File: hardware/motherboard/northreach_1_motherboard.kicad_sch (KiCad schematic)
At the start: 21 parts, among them J1 USB_C_Receptacle, J2 Conn_01x03_Pin, J3 Conn_01x20, J4 Conn_01x03_Pin, SW1 SW_Push, SW2 SW_Push, U1 TPS7A4701xRGW, U2 ESP32-S3-MINI-1U

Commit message: kicad: add LCSC parts
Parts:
- C1: LCSC (none) -> C28323
- C2, C5: LCSC (none) -> C15850
- C3, C4: LCSC (none) -> C28233
- J1: LCSC (none) -> C5119948
- J3: LCSC (none) -> C596730
- R1, R2: LCSC (none) -> C84375
- R3, R4: LCSC (none) -> C84376
- U1: LCSC (none) -> C90084
- U2: LCSC (none) -> C2980299
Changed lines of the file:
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@@
+			)
+		)
+		(property "LCSC" "C596730"
+			(at 121.92 114.3 0)
+			(effects
+				(font
+					(size 1.27 1.27)
+				)
+				(hide yes)
 			)
 		)
@@
 			)
 		)
+		(property "LCSC" "C2980299"
+			(at 232.41 113.03 0)
+			(effects
+				(font
+					(size 1.27 1.27)
+				)
+				(hide yes)
+			)
+		)
 		(pin "10"
 		)
@@
 		)
 		(property "Description" "Unpolarized capacitor"
+			(at 228.6 77.47 0)
+			(effects
+				(font
+					(size 1.27 1.27)
+				)
+				(hide yes)
+			)
+		)
+		(property "LCSC" "C28233"
 			(at 228.6 77.47 0)
 			(effects
@@
 			)
 		)
+		(property "LCSC" "C90084"
+			(at 62.23 160.02 0)
+			(effects
+				(font
+					(size 1.27 1.27)
+				)
+				(hide yes)
+			)
+		)
 		(pin "1"
 		)
@@
 			)
 		)
+		(property "LCSC" "C5119948"
+			(at 45.72 67.31 0)
+			(effects
+				(font
+					(size 1.27 1.27)
+				)
+				(hide yes)
+			)
+		)
 		(pin "A11"
 		)
@@
 			)
 		)
+		(property "LCSC" "C84375"
+			(at 73.66 45.72 90)
+			(effects
+				(font
+					(size 1.27 1.27)
+				)
+				(hide yes)
+			)
+		)
 		(pin "2"
 		)
@@
 		)
 		(property "Description" "Unpolarized capacitor"
+			(at 125.73 40.64 0)
+			(effects
+				(font
+					(size 1.27 1.27)
+				)
+				(hide yes)
+			)
+		)
+		(property "LCSC" "C28233"
 			(at 125.73 40.64 0)
 			(effects
@@
 			)
 		)
+		(property "LCSC" "C84376"
+			(at 118.11 35.56 90)
+			(effects
+				(font
+					(size 1.27 1.27)
+				)
+				(hide yes)
+			)
+		)
 		(pin "2"
 		)
@@
 			)
 		)
+		(property "LCSC" "C84376"
+			(at 123.19 58.42 90)
+			(effects
+				(font
+					(size 1.27 1.27)
+				)
+				(hide yes)
+			)
+		)
 		(pin "2"
 		)
@@
 			)
 		)
+		(property "LCSC" "C15850"
+			(at 228.6 66.04 0)
+			(effects
+				(font
+					(size 1.27 1.27)
+				)
+				(hide yes)
+			)
+		)
 		(pin "1"
 		)
@@
 			)
 		)
+		(property "LCSC" "C84375"
+			(at 73.66 50.8 90)
+			(effects
+				(font
+					(size 1.27 1.27)
+				)
+				(hide yes)
+			)
+		)
 		(pin "2"
 		)
@@
 			)
 		)
+		(property "LCSC" "C28323"
+			(at 77.47 173.99 0)
+			(effects
+				(font
+					(size 1.27 1.27)
+				)
+				(hide yes)
+			)
+		)
 		(pin "1"
 		)
@@
 			(at 38.1 153.67 0)
 			(effects
+				(font
+					(size 1.27 1.27)
+				)
+				(hide yes)
+			)
+		)
+		(property "LCSC" "C15850"
+			(at 38.1 153.67 0)
+			(effects

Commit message: schematic: motherboard: change switch footprint for EN and RESET
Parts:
- SW1, SW2: footprint Button_Switch_THT:SW_PUSH_6mm_H5mm -> Button_Switch_THT:SW_PUSH_6mm_H4.3mm
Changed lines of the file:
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@@
 			)
 		)
-		(property "Footprint" "Button_Switch_THT:SW_PUSH_6mm_H5mm"
+		(property "Footprint" "Button_Switch_THT:SW_PUSH_6mm_H4.3mm"
 			(at 137.16 40.64 0)
 			(effects
@@
 			)
 		)
-		(property "Footprint" "Button_Switch_THT:SW_PUSH_6mm_H5mm"
+		(property "Footprint" "Button_Switch_THT:SW_PUSH_6mm_H4.3mm"
 			(at 128.27 64.77 0)
 			(effects

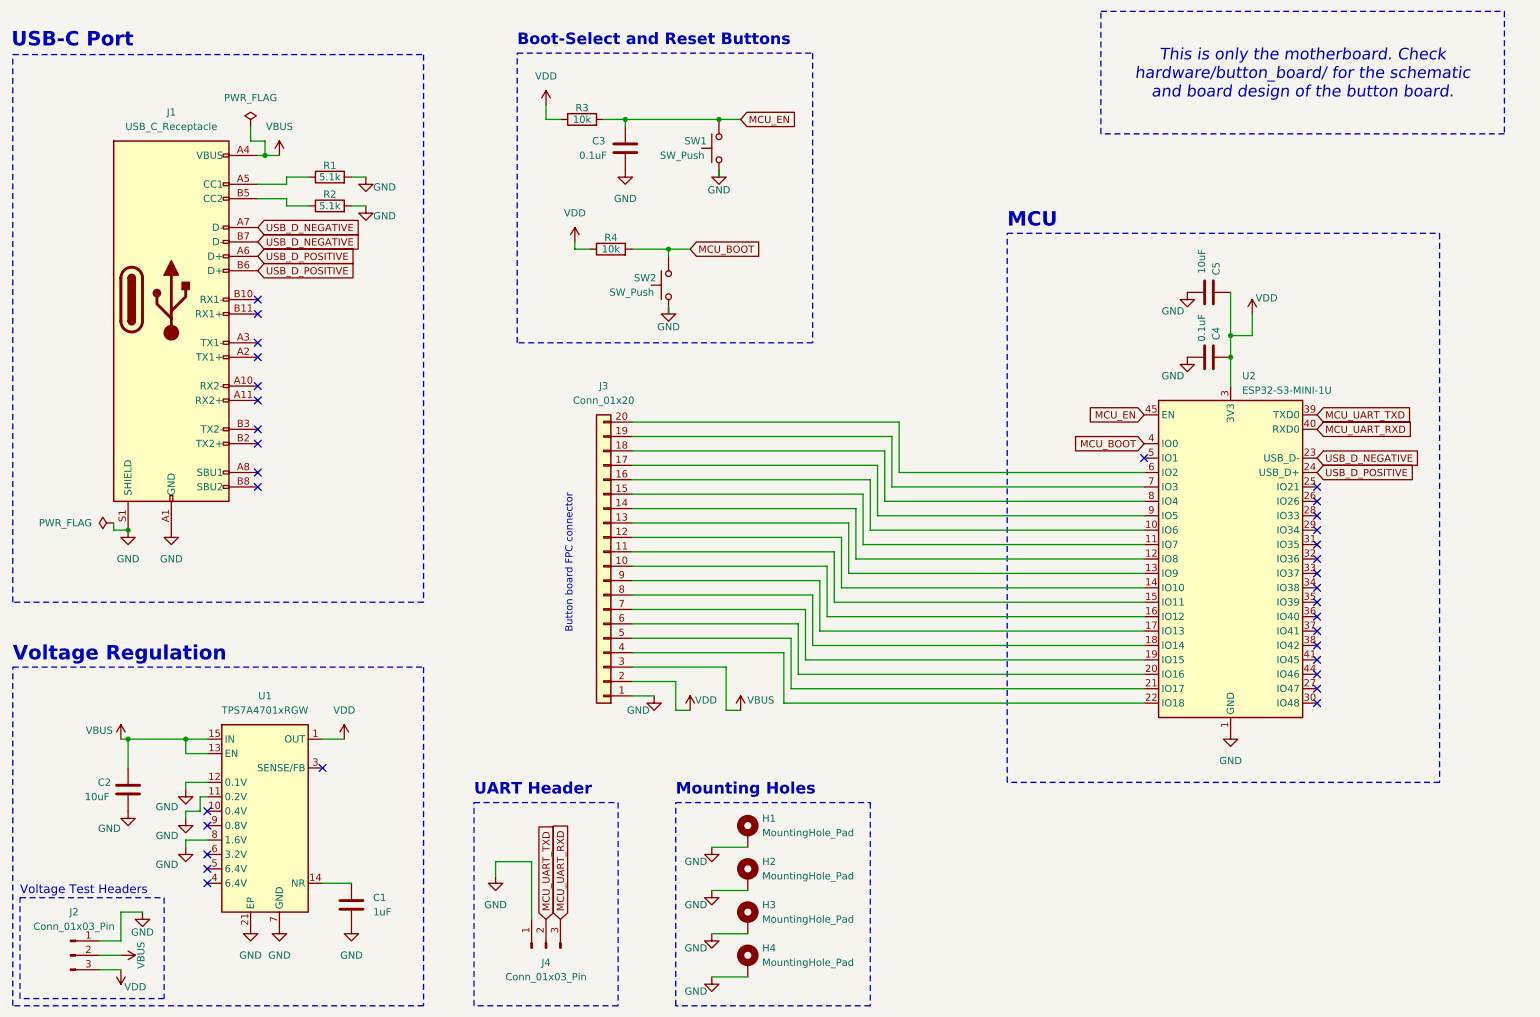
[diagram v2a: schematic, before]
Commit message: schematic: motherboard: add usb esd protection
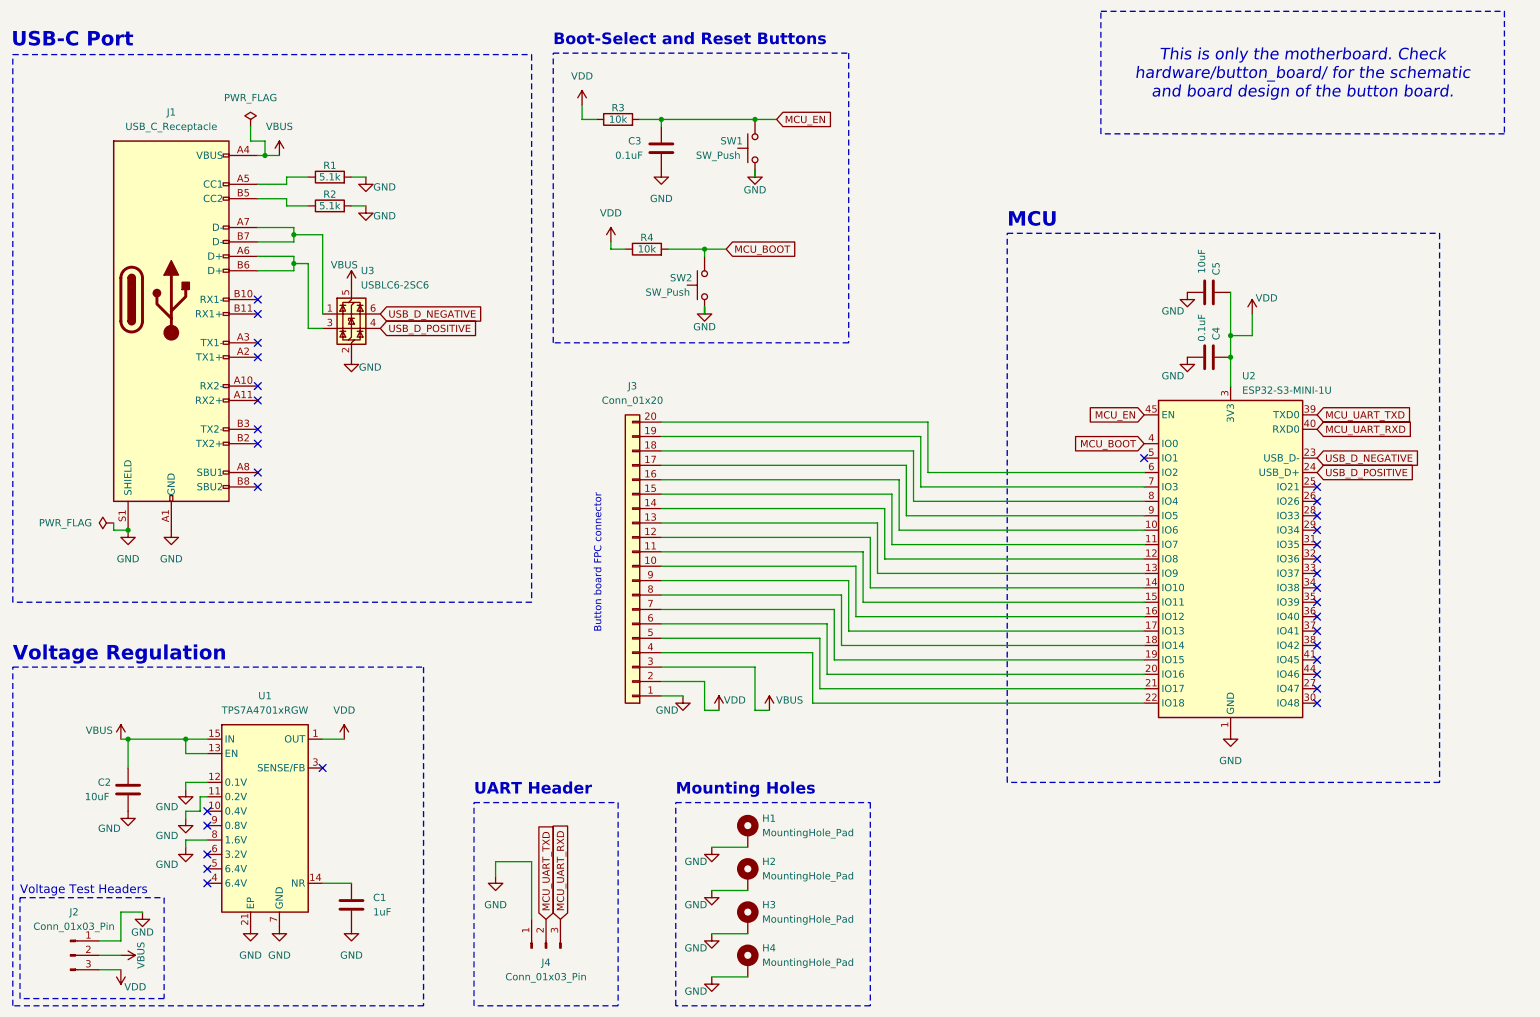
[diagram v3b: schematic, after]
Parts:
- added U3: USBLC6-2SC6, Package_TO_SOT_SMD:SOT-23-6, symbol Power_Protection:USBLC6-2SC6
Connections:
- net GND: now also U3.2 (GND)
- net USB_D_NEGATIVE: now also U3.6 (I/O1); no longer J1.A7 (D-), J1.B7 (D-)
- net USB_D_POSITIVE: now also U3.4 (I/O2); no longer J1.A6 (D+), J1.B6 (D+)
- net VBUS: now also U3.5 (VBUS)
- new net: J1.A6 (D+), J1.B6 (D+), U3.3 (I/O2)
- new net: J1.A7 (D-), J1.B7 (D-), U3.1 (I/O1)
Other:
- moved on the sheet: C3, J3, R3, R4, SW1, SW2

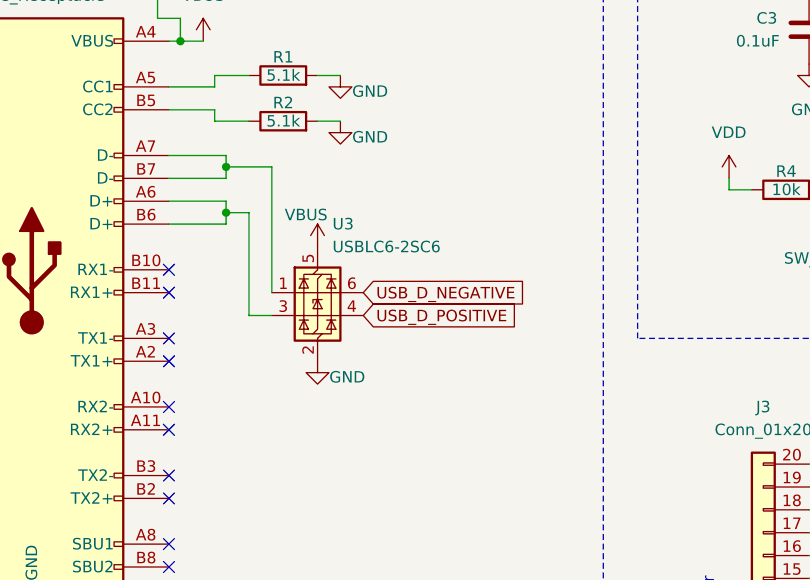
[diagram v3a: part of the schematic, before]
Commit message: schematic: motherboard: text, drawing sheet details
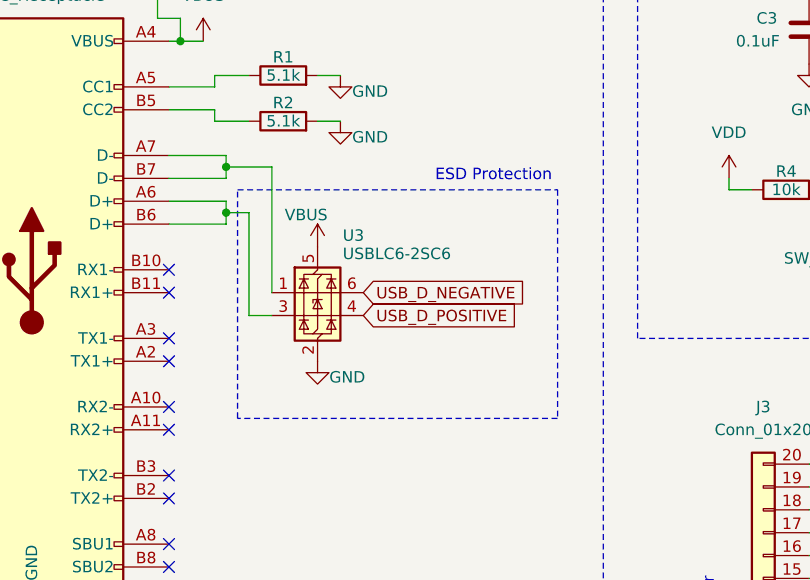
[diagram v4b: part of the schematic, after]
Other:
- note added: "ESD Protection"
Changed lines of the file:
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@@
 	(title_block
 		(title "NorthReach 1 - Motherboard")
-		(date "2026-01-08")
+		(date "2026-01-24")
 		(rev "v1.0")
 		(company "Stratos Thivaios")
@@
 	)
 	(rectangle
+		(start 68.58 58.42)
+		(end 104.14 83.82)
+		(stroke
+			(width 0)
+			(type dash_dot)
+			(color 0 1 255 1)
+		)
+		(fill
+			(type none)
+		)
+	)
+	(rectangle
 		(start 17.78 132.08)
 		(end 90.17 191.77)
@@
 		)
 	)
+	(text "ESD Protection"
+		(exclude_from_sim no)
+		(at 97.028 56.896 0)
+		(effects
+			(font
+				(size 1.27 1.27)
+			)
+		)
+	)
 	(text "USB-C Port"
 		(exclude_from_sim no)
@@
 		(on_board yes)
 		(dnp no)
-		(fields_autoplaced yes)
 		(property "Reference" "U3"
-			(at 79.1211 62.23 0)
+			(at 80.264 63.5 0)
 			(effects
 				(font
@@
 		)
 		(property "Value" "USBLC6-2SC6"
-			(at 79.1211 64.77 0)
+			(at 80.264 65.532 0)
 			(effects
 				(font

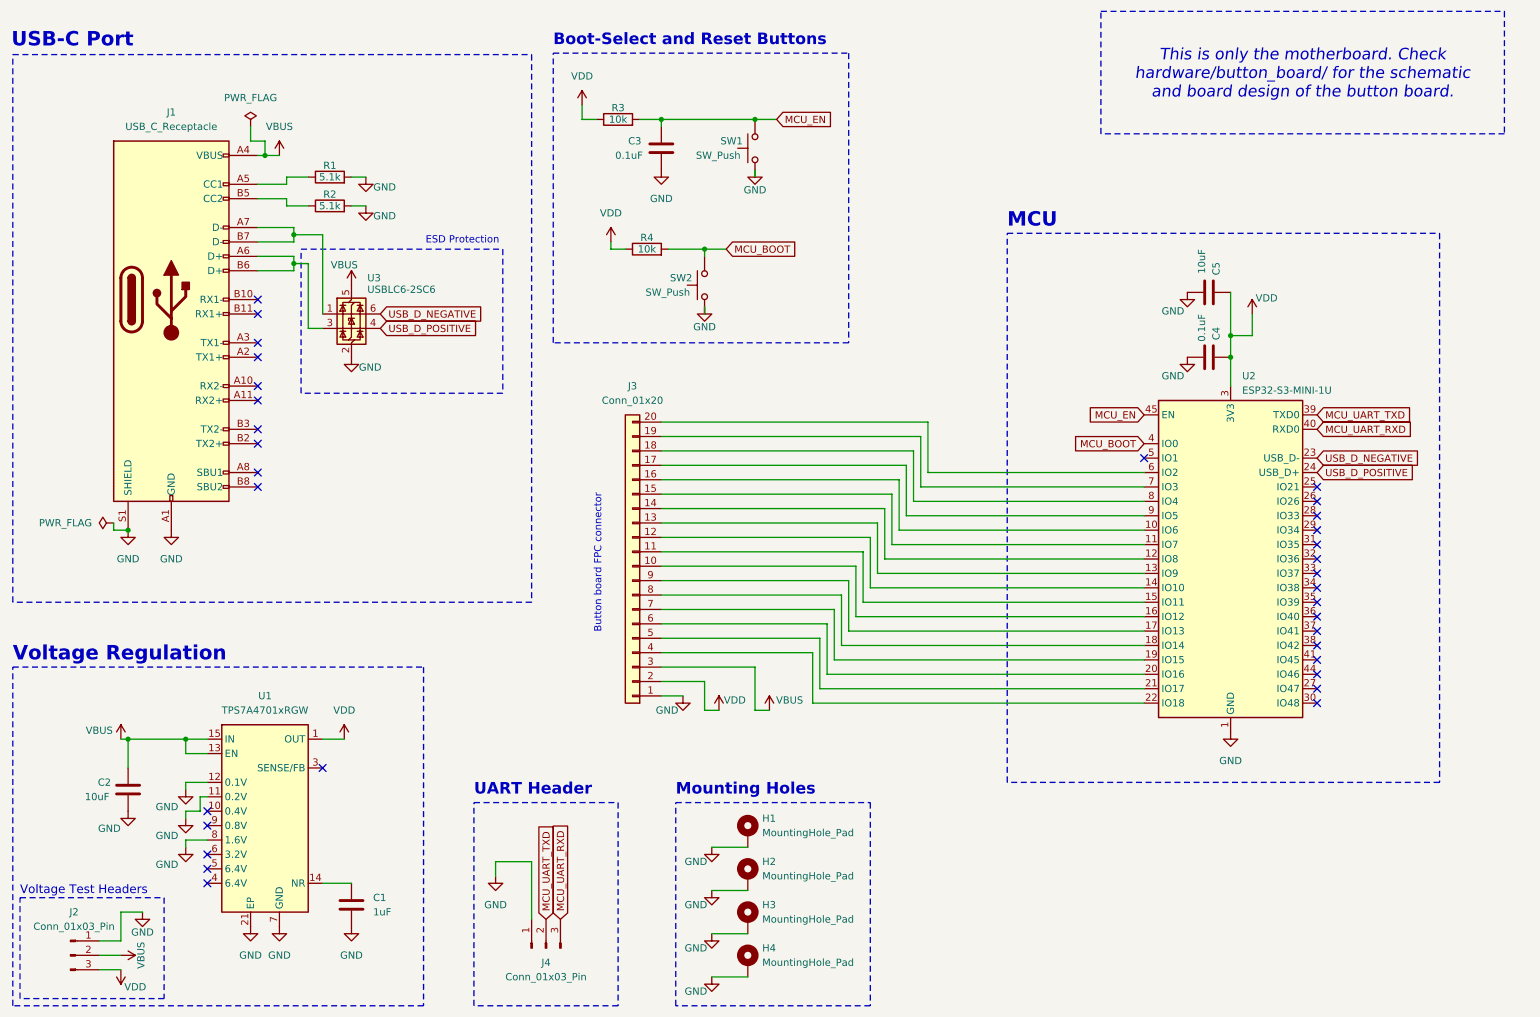
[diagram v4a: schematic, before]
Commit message: schematic_and_pcb: motherboard: route SENSE VREG pin to load
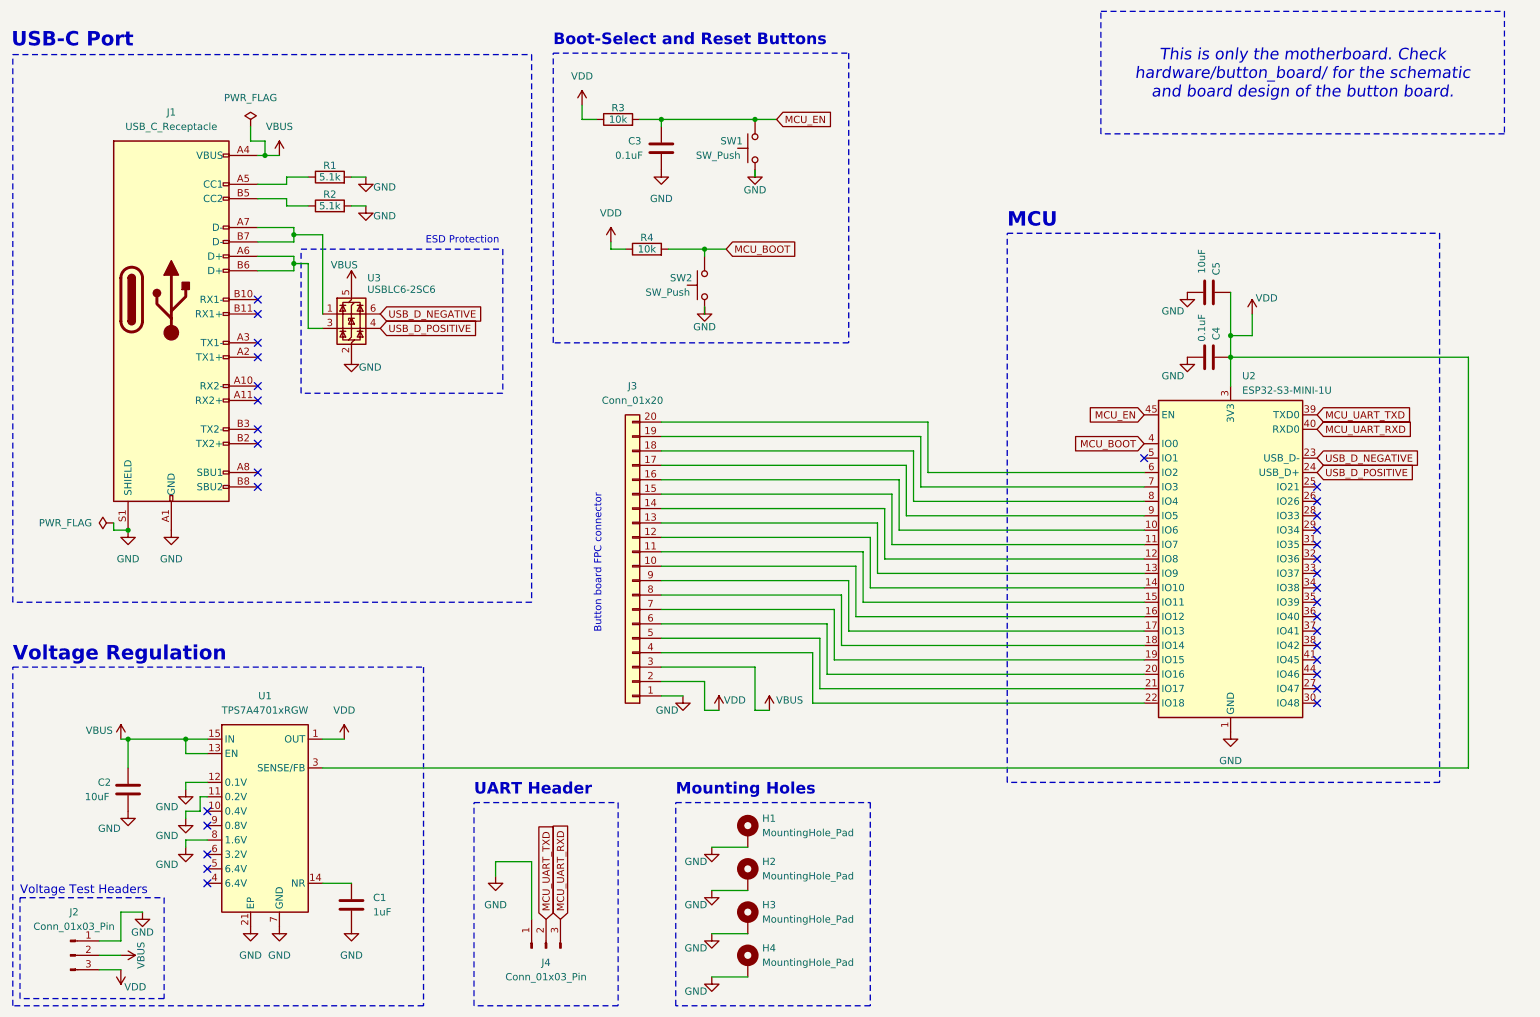
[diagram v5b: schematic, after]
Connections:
- net VDD: now also U1.3 (SENSE/FB)
- no-connect marks 33 -> 32
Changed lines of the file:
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@@
-	)
-	(no_connect
-		(at 72.39 149.86)
 	)
 	(no_connect
@@
 	(wire
 		(pts
+			(xy 274.32 149.86) (xy 72.39 149.86)
+		)
+		(stroke
+			(width 0)
+			(type default)
+		)
+	)
+	(wire
+		(pts
 			(xy 132.08 106.68) (xy 170.18 106.68)
 		)
@@
 	(wire
 		(pts
+			(xy 232.41 77.47) (xy 274.32 77.47)
+		)
+		(stroke
+			(width 0)
+			(type default)
+		)
+	)
+	(wire
+		(pts
 			(xy 232.41 73.66) (xy 232.41 77.47)
 		)
@@
 		)
 		(stroke
+			(width 0)
+			(type default)
+		)
+	)
+	(wire
+		(pts
+			(xy 274.32 77.47) (xy 274.32 149.86)
+		)
+		(stroke

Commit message: schematic_and_pcb: motherboard: add ESD protection IC LCSC id
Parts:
- U3: LCSC (none) -> C7519
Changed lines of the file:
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@@
+			)
+		)
+		(property "LCSC" "C7519"
+			(at 77.47 69.85 0)
+			(effects
+				(font
+					(size 1.27 1.27)
+				)
+				(hide yes)
 			)
 		)
